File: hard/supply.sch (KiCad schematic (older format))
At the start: 14 parts, among them J2 MicroXNJ

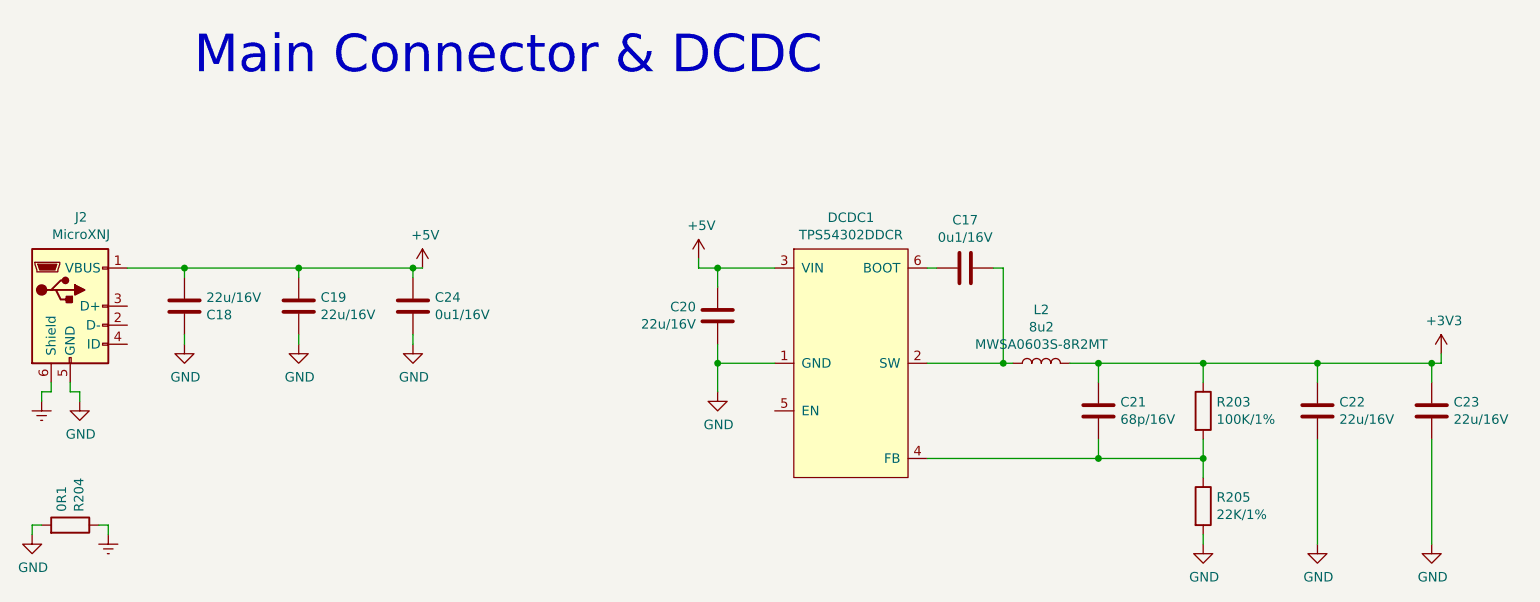
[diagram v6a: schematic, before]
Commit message: re-connect footprints
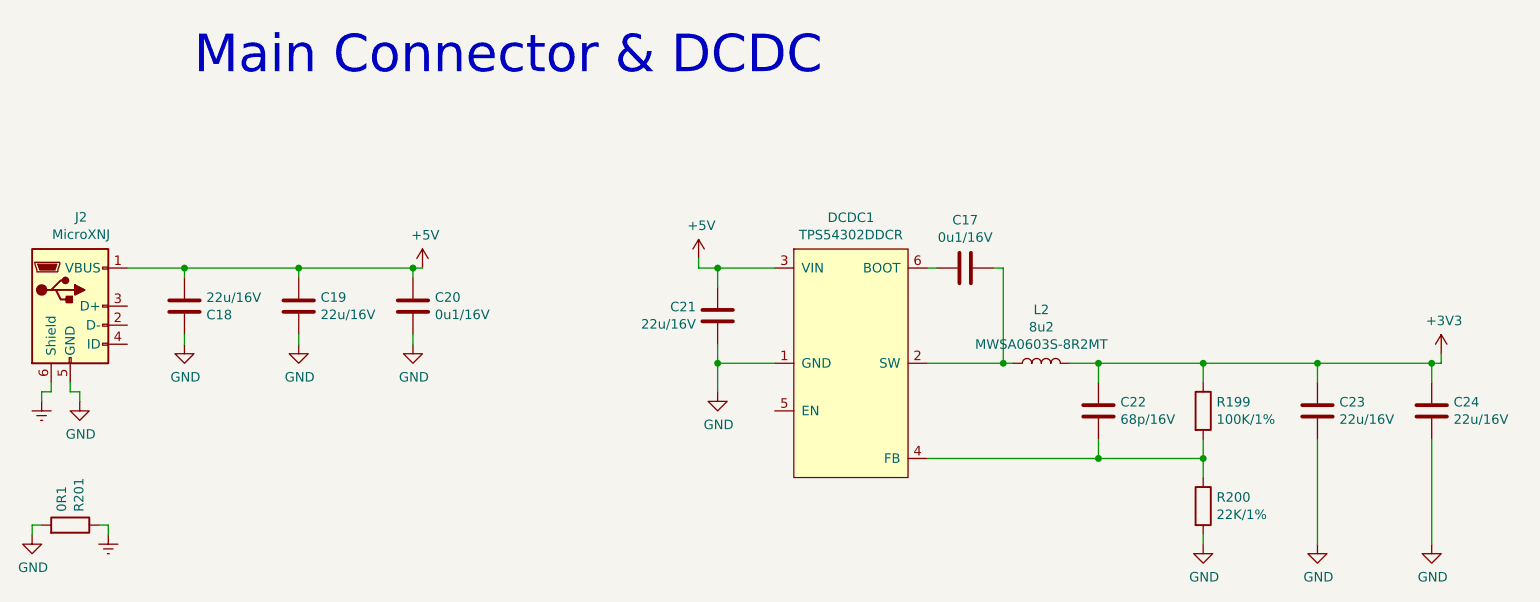
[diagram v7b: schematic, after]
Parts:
- renumbered C24 to C20, C20 to C21, C21 to C22, C22 to C23, C23 to C24, R203 to R199, R205 to R200, R204 to R201
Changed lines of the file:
@@
 $EndComp
 $Comp
-L Device:C C20
+L Device:C C21
 U 1 1 6055E066
 P 5850 3650
-F 0 "C20" H 5736 3604 50  0000 R CNN
+F 0 "C21" H 5736 3604 50  0000 R CNN
 F 1 "22u/16V" H 5736 3695 50  0000 R CNN
 F 2 "Capacitor_SMD:C_0805_2012Metric" H 5888 3500 50  0001 C CNN
@@
 $EndComp
 $Comp
-L Device:C C21
+L Device:C C22
 U 1 1 60563587
 P 7850 4150
-F 0 "C21" H 7735 4104 50  0000 R CNN
+F 0 "C22" H 7735 4104 50  0000 R CNN
 F 1 "68p/16V" H 7735 4195 50  0000 R CNN
 F 2 "Capacitor_SMD:C_0402_1005Metric" H 7888 4000 50  0001 C CNN
@@
 $EndComp
 $Comp
-L Device:R R203
+L Device:R R199
 U 1 1 6056BF47
 P 8400 4150
-F 0 "R203" H 8470 4196 50  0000 L CNN
+F 0 "R199" H 8470 4196 50  0000 L CNN
 F 1 "100K/1%" H 8470 4105 50  0000 L CNN
 F 2 "Resistor_SMD:R_0402_1005Metric" V 8330 4150 50  0001 C CNN
@@
 $EndComp
 $Comp
-L Device:R R205
+L Device:R R200
 U 1 1 6056F7CE
 P 8400 4650
-F 0 "R205" H 8470 4696 50  0000 L CNN
+F 0 "R200" H 8470 4696 50  0000 L CNN
 F 1 "22K/1%" H 8470 4605 50  0000 L CNN
 F 2 "Resistor_SMD:R_0402_1005Metric" V 8330 4650 50  0001 C CNN
@@
 $EndComp
 $Comp
-L Device:C C22
+L Device:C C23
 U 1 1 60572E18
 P 9000 4150
-F 0 "C22" H 8885 4104 50  0000 R CNN
+F 0 "C23" H 8885 4104 50  0000 R CNN
 F 1 "22u/16V" H 8885 4195 50  0000 R CNN
 F 2 "Capacitor_SMD:C_0805_2012Metric" H 9038 4000 50  0001 C CNN
@@
 $EndComp
 $Comp
-L Device:C C23
+L Device:C C24
 U 1 1 60574B19
 P 9600 4150
-F 0 "C23" H 9485 4104 50  0000 R CNN
+F 0 "C24" H 9485 4104 50  0000 R CNN
 F 1 "22u/16V" H 9485 4195 50  0000 R CNN
 F 2 "Capacitor_SMD:C_0805_2012Metric" H 9638 4000 50  0001 C CNN
@@
 $EndComp
 $Comp
-L power:+3V3 #PWR0191
+L power:+3V3 #PWR0189
 U 1 1 60578BC3
 P 9650 3850
-F 0 "#PWR0191" H 9650 3700 50  0001 C CNN
+F 0 "#PWR0189" H 9650 3700 50  0001 C CNN
 F 1 "+3V3" H 9665 4023 50  0000 C CNN
 F 2 "" H 9650 3850 50  0001 C CNN
@@
 	7350 3900 6950 3900
 $Comp
-L power:+5V #PWR0188
+L power:+5V #PWR0184
 U 1 1 6057B855
 P 5750 3350
-F 0 "#PWR0188" H 5750 3200 50  0001 C CNN
+F 0 "#PWR0184" H 5750 3200 50  0001 C CNN
 F 1 "+5V" H 5765 3523 50  0000 C CNN
 F 2 "" H 5750 3350 50  0001 C CNN
@@
 	5850 3900 5850 3800
 $Comp
-L power:GND #PWR0192
+L power:GND #PWR0190
 U 1 1 60575673
 P 5850 4050
-F 0 "#PWR0192" H 5850 3800 50  0001 C CNN
+F 0 "#PWR0190" H 5850 3800 50  0001 C CNN
 F 1 "GND" H 5855 3877 50  0000 C CNN
 F 2 "" H 5850 4050 50  0001 C CNN
@@
 	6950 4400 7850 4400
 $Comp
-L power:GND #PWR0198
+L power:GND #PWR0196
 U 1 1 605811D8
 P 9000 4850
-F 0 "#PWR0198" H 9000 4600 50  0001 C CNN
+F 0 "#PWR0196" H 9000 4600 50  0001 C CNN
 F 1 "GND" H 9005 4677 50  0000 C CNN
 F 2 "" H 9000 4850 50  0001 C CNN
@@
 Connection ~ 9000 3900
 $Comp
-L power:GND #PWR0199
+L power:GND #PWR0197
 U 1 1 605828FA
 P 9600 4850
-F 0 "#PWR0199" H 9600 4600 50  0001 C CNN
+F 0 "#PWR0197" H 9600 4600 50  0001 C CNN
 F 1 "GND" H 9605 4677 50  0000 C CNN
 F 2 "" H 9600 4850 50  0001 C CNN
@@
 $EndComp
 $Comp
-L power:GND #PWR0197
+L power:GND #PWR0195
 U 1 1 6057A1D3
 P 8400 4850
-F 0 "#PWR0197" H 8400 4600 50  0001 C CNN
+F 0 "#PWR0195" H 8400 4600 50  0001 C CNN
 F 1 "GND" H 8405 4677 50  0000 C CNN
 F 2 "" H 8400 4850 50  0001 C CNN
@@
 $EndComp
 $Comp
-L power:+5V #PWR0187
+L power:+5V #PWR0185
 U 1 1 6056C9AF
 P 4300 3400
-F 0 "#PWR0187" H 4300 3250 50  0001 C CNN
+F 0 "#PWR0185" H 4300 3250 50  0001 C CNN
 F 1 "+5V" H 4315 3573 50  0000 C CNN
 F 2 "" H 4300 3400 50  0001 C CNN
@@
 $EndComp
 $Comp
-L power:GND #PWR0194
+L power:GND #PWR0192
 U 1 1 6056D447
 P 2500 4100
-F 0 "#PWR0194" H 2500 3850 50  0001 C CNN
+F 0 "#PWR0192" H 2500 3850 50  0001 C CNN
 F 1 "GND" H 2505 3927 50  0000 C CNN
 F 2 "" H 2500 4100 50  0001 C CNN
@@
 	3050 3400 3650 3400
 $Comp
-L power:GND #PWR0189
+L power:GND #PWR0186
 U 1 1 6057E614
 P 3050 3800
-F 0 "#PWR0189" H 3050 3550 50  0001 C CNN
+F 0 "#PWR0186" H 3050 3550 50  0001 C CNN
 F 1 "GND" H 3055 3627 50  0000 C CNN
 F 2 "" H 3050 3800 50  0001 C CNN
@@
 $EndComp
 $Comp
-L power:GND #PWR0190
+L power:GND #PWR0187
 U 1 1 6057ED88
 P 3650 3800
-F 0 "#PWR0190" H 3650 3550 50  0001 C CNN
+F 0 "#PWR0187" H 3650 3550 50  0001 C CNN
 F 1 "GND" H 3655 3627 50  0000 C CNN
 F 2 "" H 3650 3800 50  0001 C CNN
@@
 	2450 4000 2450 4050
 $Comp
-L power:Earth #PWR0193
+L power:Earth #PWR0191
 U 1 1 614F2C5D
 P 2300 4100
-F 0 "#PWR0193" H 2300 3850 50  0001 C CNN
+F 0 "#PWR0191" H 2300 3850 50  0001 C CNN
 F 1 "Earth" H 2300 3950 50  0001 C CNN
 F 2 "" H 2300 4100 50  0001 C CNN
@@
 	4250 3400 4300 3400
 $Comp
-L power:GND #PWR0200
+L power:GND #PWR0188
 U 1 1 613BB852
 P 4250 3800
-F 0 "#PWR0200" H 4250 3550 50  0001 C CNN
+F 0 "#PWR0188" H 4250 3550 50  0001 C CNN
 F 1 "GND" H 4255 3627 50  0000 C CNN
 F 2 "" H 4250 3800 50  0001 C CNN
@@
 	4250 3750 4250 3800
 $Comp
-L Device:C C24
+L Device:C C20
 U 1 1 613D470A
 P 4250 3600
-F 0 "C24" H 4135 3554 50  0000 R CNN
+F 0 "C20" H 4135 3554 50  0000 R CNN
 F 1 "0u1/16V" H 4135 3645 50  0000 R CNN
 F 2 "Capacitor_SMD:C_0402_1005Metric" H 4288 3450 50  0001 C CNN
@@
 	2250 4800 2250 4750
 $Comp
-L power:GND #PWR0195
+L power:GND #PWR0193
 U 1 1 614F0A85
 P 2250 4800
-F 0 "#PWR0195" H 2250 4550 50  0001 C CNN
+F 0 "#PWR0193" H 2250 4550 50  0001 C CNN
 F 1 "GND" H 2255 4627 50  0000 C CNN
 F 2 "" H 2250 4800 50  0001 C CNN
@@
 $EndComp
 $Comp
-L power:Earth #PWR0196
+L power:Earth #PWR0194
 U 1 1 614EE00A
 P 2650 4800
-F 0 "#PWR0196" H 2650 4550 50  0001 C CNN
+F 0 "#PWR0194" H 2650 4550 50  0001 C CNN
 F 1 "Earth" H 2650 4650 50  0001 C CNN
 F 2 "" H 2650 4800 50  0001 C CNN
@@
 $EndComp
 $Comp
-L Device:R R204
+L Device:R R201
 U 1 1 6056E34B
 P 2450 4750
-F 0 "R204" H 2520 4796 50  0000 L CNN
+F 0 "R201" H 2520 4796 50  0000 L CNN
 F 1 "0R1" H 2520 4705 50  0000 L CNN
 F 2 "Resistor_SMD:R_0805_2012Metric" V 2380 4750 50  0001 C CNN

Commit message: updated footprints in preparation for connector 3d files
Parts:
- J2: footprint led_matrix:Connectors_SHOU HAN_MICRO 4P DIP -> led_matrix:Connectors_SHOU-HAN_MICRO-4P-DIP
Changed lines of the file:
@@
 F 0 "J2" H 2507 4067 50  0000 C CNN
 F 1 "MicroXNJ" H 2507 3976 50  0000 C CNN
-F 2 "led_matrix:Connectors_SHOU HAN_MICRO 4P DIP" H 2600 3550 50  0001 C CNN
+F 2 "led_matrix:Connectors_SHOU-HAN_MICRO-4P-DIP" H 2600 3550 50  0001 C CNN
 F 3 "https://datasheet.lcsc.com/szlcsc/1912111437_SHOU-HAN-MICRO-4P-DIP_C456008.pdf" H 2600 3550 50  0001 C CNN
 F 4 "" H 2450 3600 50  0001 C CNN "DigiKey"
